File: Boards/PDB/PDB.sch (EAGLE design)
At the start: 47 parts, among them Q1 NMOS, Q2 IRFML8244, Q3 PMOS, Q4 PMOS, Q5 PMOS

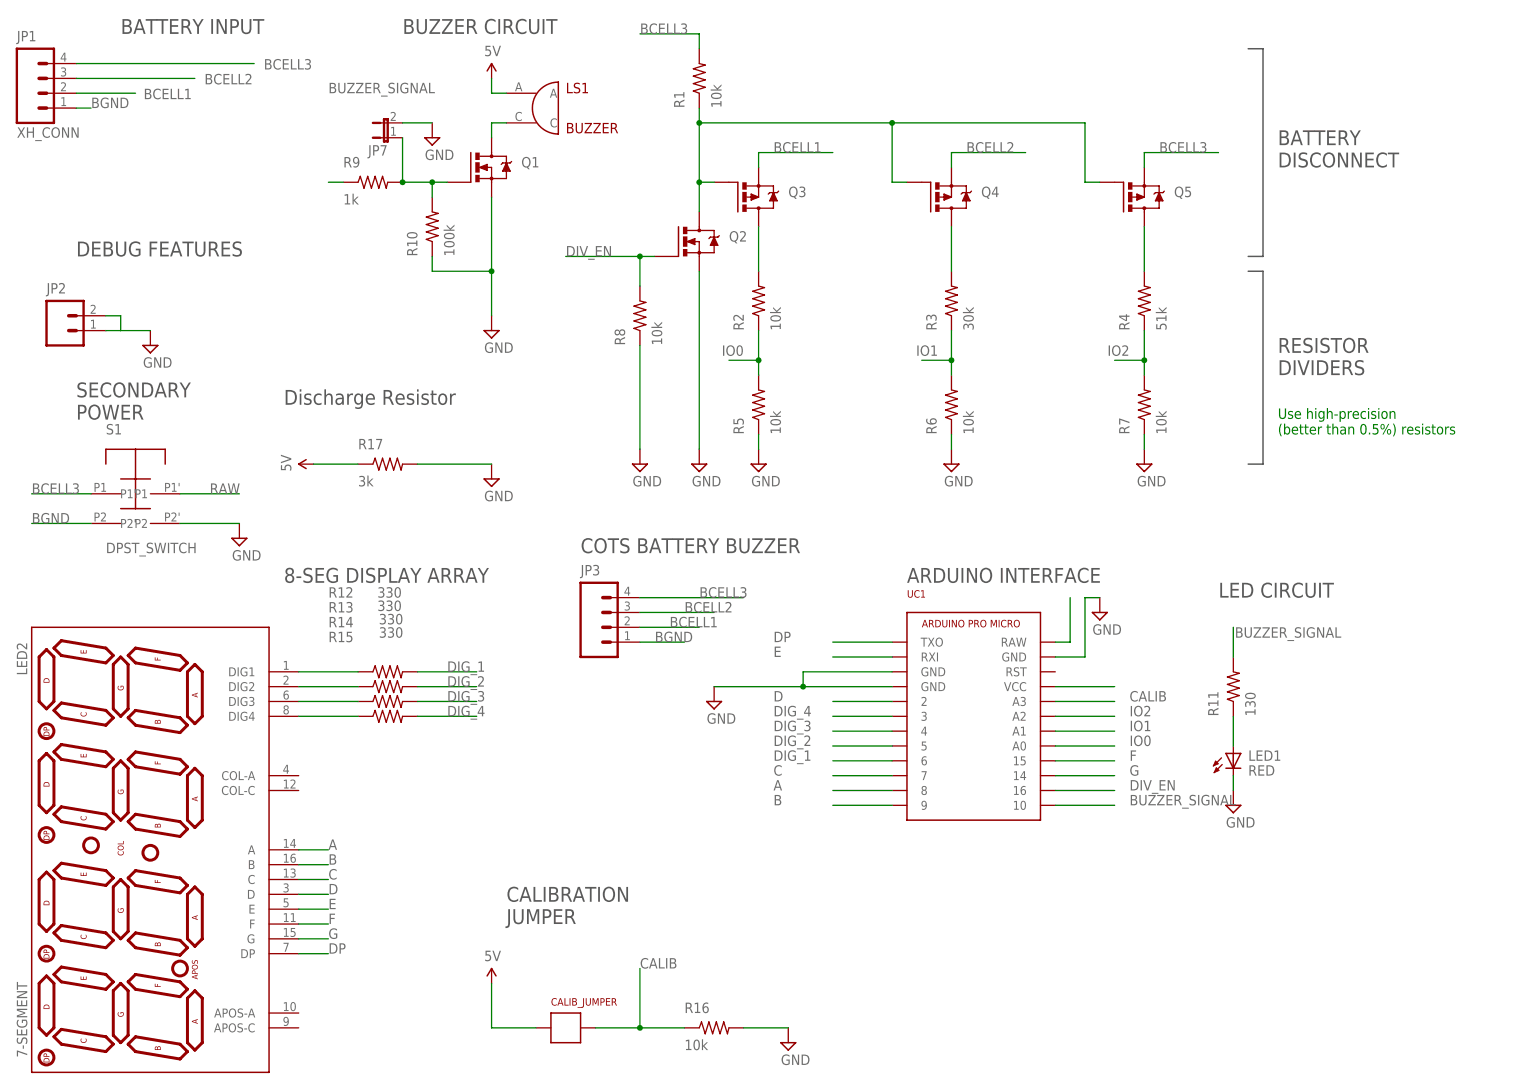
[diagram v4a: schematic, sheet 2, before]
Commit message: Please, PDB, please work. Also I updated ATX connector.
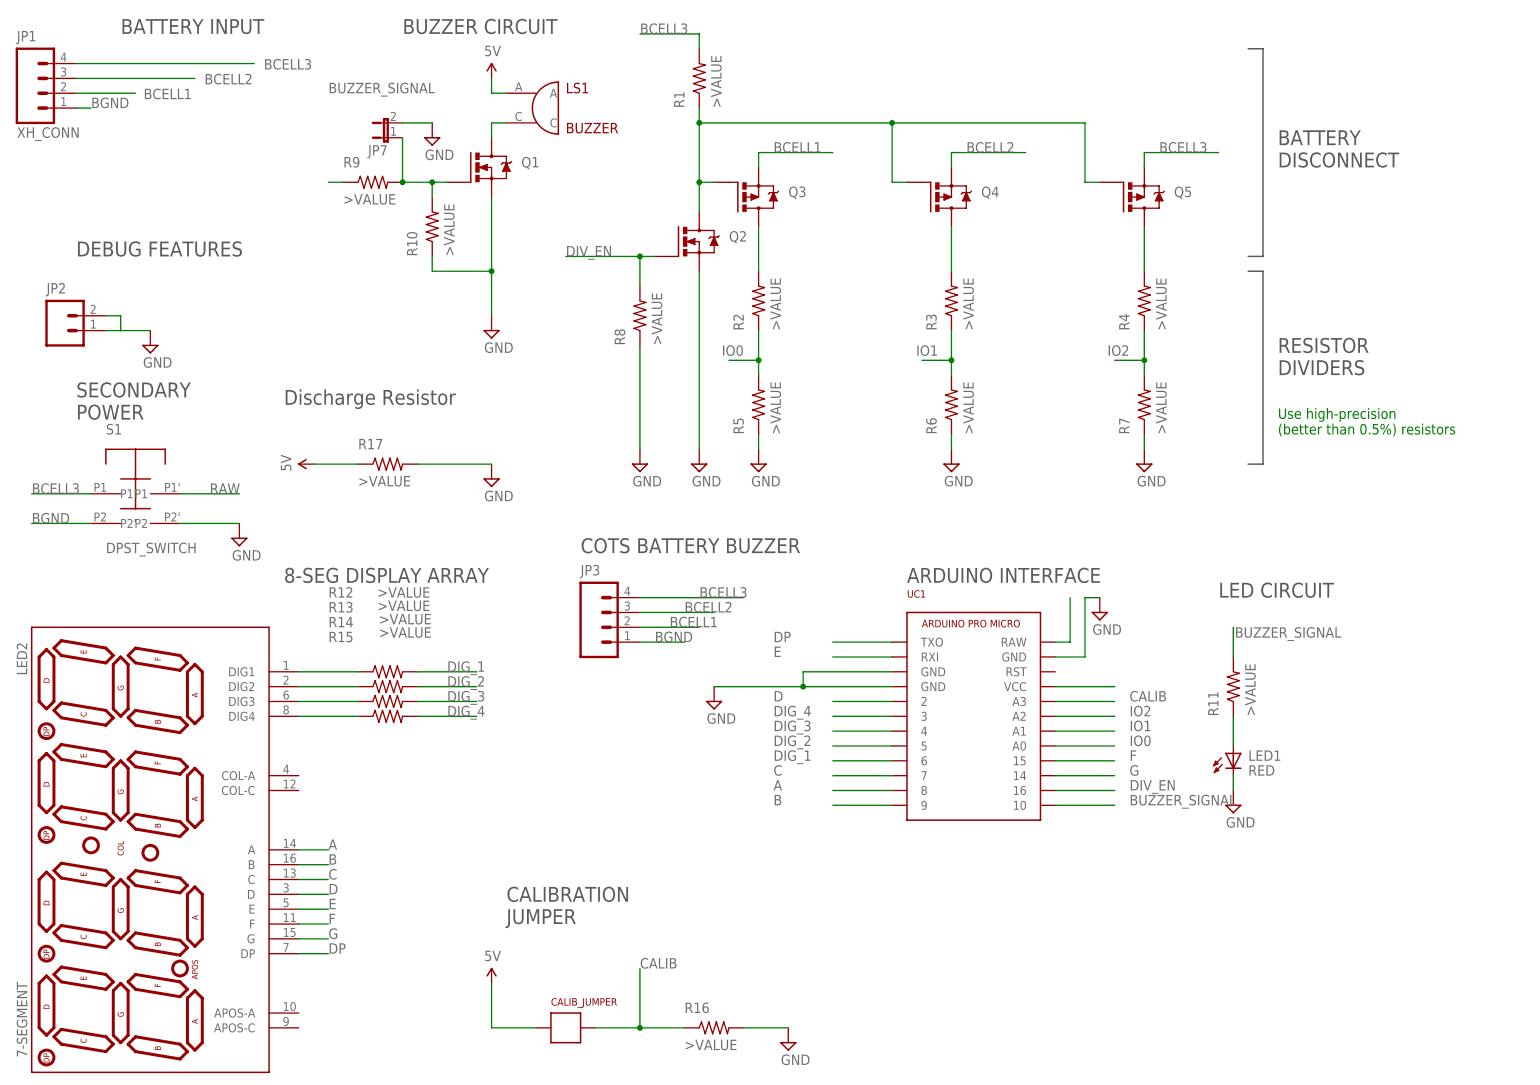
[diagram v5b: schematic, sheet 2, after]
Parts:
- R1, R16, R2, R5, R6, R7, R8: value 10k -> >VALUE
- R10: value 100k -> >VALUE
- R11: value 130 -> >VALUE
- R12, R13, R14, R15: value 330 -> >VALUE
- R17: value 3k -> >VALUE
- R3: value 30k -> >VALUE
- R4: value 51k -> >VALUE
- R9: value 1k -> >VALUE
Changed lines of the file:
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@@
 </part>
 <part name="JP1" library="pie" deviceset="XH_CONNECTOR_4POS" device="" value="XH_CONN"/>
-<part name="R2" library="pie" deviceset="R-US_" device="R0603" value="10k"/>
-<part name="R3" library="pie" deviceset="R-US_" device="R0603" value="30k"/>
-<part name="R4" library="pie" deviceset="R-US_" device="R0603" value="51k"/>
-<part name="R5" library="pie" deviceset="R-US_" device="R0603" value="10k"/>
-<part name="R6" library="pie" deviceset="R-US_" device="R0603" value="10k"/>
-<part name="R7" library="pie" deviceset="R-US_" device="R0603" value="10k"/>
+<part name="R2" library="pie" deviceset="R-US_" device="R0603" value="&gt;VALUE"/>
+<part name="R3" library="pie" deviceset="R-US_" device="R0603" value="&gt;VALUE"/>
+<part name="R4" library="pie" deviceset="R-US_" device="R0603" value="&gt;VALUE"/>
+<part name="R5" library="pie" deviceset="R-US_" device="R0603" value="&gt;VALUE"/>
+<part name="R6" library="pie" deviceset="R-US_" device="R0603" value="&gt;VALUE"/>
+<part name="R7" library="pie" deviceset="R-US_" device="R0603" value="&gt;VALUE"/>
 <part name="SUPPLY14" library="pie" deviceset="GND" device=""/>
 <part name="SUPPLY15" library="pie" deviceset="GND" device=""/>
 <part name="SUPPLY16" library="pie" deviceset="GND" device=""/>
 <part name="LS1" library="pie" deviceset="BUZZER" device="" value="BUZZER"/>
-<part name="R9" library="pie" deviceset="R-US_" device="R0603" value="1k"/>
-<part name="R10" library="pie" deviceset="R-US_" device="R0603" value="100k"/>
+<part name="R9" library="pie" deviceset="R-US_" device="R0603" value="&gt;VALUE"/>
+<part name="R10" library="pie" deviceset="R-US_" device="R0603" value="&gt;VALUE"/>
 <part name="U$12" library="pie" deviceset="5V" device=""/>
 <part name="SUPPLY17" library="pie" deviceset="GND" device=""/>
-<part name="R11" library="pie" deviceset="R-US_" device="R0603" value="130"/>
+<part name="R11" library="pie" deviceset="R-US_" device="R0603" value="&gt;VALUE"/>
 <part name="LED1" library="pie" deviceset="LED" device="0805" value="RED"/>
 <part name="SUPPLY18" library="pie" deviceset="GND" device=""/>
@@
 <part name="Q3" library="pie" deviceset="P-CHANNEL-MOSFET" device="SOT23-3" value="PMOS"/>
 <part name="Q2" library="pie" deviceset="N-CHANNEL-MOSFET" device="SOT23-3" value="IRFML8244"/>
-<part name="R1" library="pie" deviceset="R-US_" device="R0603" value="10k"/>
+<part name="R1" library="pie" deviceset="R-US_" device="R0603" value="&gt;VALUE"/>
 <part name="SUPPLY19" library="pie" deviceset="GND" device=""/>
-<part name="R8" library="pie" deviceset="R-US_" device="R0603" value="10k"/>
+<part name="R8" library="pie" deviceset="R-US_" device="R0603" value="&gt;VALUE"/>
 <part name="SUPPLY20" library="pie" deviceset="GND" device=""/>
 <part name="Q1" library="pie" deviceset="N-CHANNEL-MOSFET" device="SOT23-3" value="NMOS"/>
@@
 <part name="SUPPLY21" library="pie" deviceset="GND" device=""/>
 <part name="SUPPLY22" library="pie" deviceset="GND" device=""/>
-<part name="R13" library="pie" deviceset="R-US_" device="R0603" value="330"/>
-<part name="R14" library="pie" deviceset="R-US_" device="R0603" value="330"/>
-<part name="R12" library="pie" deviceset="R-US_" device="R0603" value="330"/>
-<part name="R15" library="pie" deviceset="R-US_" device="R0603" value="330"/>
+<part name="R13" library="pie" deviceset="R-US_" device="R0603" value="&gt;VALUE"/>
+<part name="R14" library="pie" deviceset="R-US_" device="R0603" value="&gt;VALUE"/>
+<part name="R12" library="pie" deviceset="R-US_" device="R0603" value="&gt;VALUE"/>
+<part name="R15" library="pie" deviceset="R-US_" device="R0603" value="&gt;VALUE"/>
 <part name="U$9" library="pie" deviceset="5V" device=""/>
-<part name="R16" library="pie" deviceset="R-US_" device="R0603" value="10k"/>
+<part name="R16" library="pie" deviceset="R-US_" device="R0603" value="&gt;VALUE"/>
 <part name="SUPPLY23" library="pie" deviceset="GND" device=""/>
 <part name="SUPPLY24" library="pie" deviceset="GND" device=""/>
@@
 <part name="SUPPLY26" library="pie" deviceset="GND" device=""/>
 <part name="APM_5V1" library="pie" deviceset="5V" device=""/>
-<part name="R17" library="pie" deviceset="R-US_" device="R0603" value="3k"/>
-<part name="JP7" library="jumper" deviceset="JP1E" device=""/>
+<part name="R17" library="pie" deviceset="R-US_" device="R0603" value="&gt;VALUE"/>
+<part name="JP7" library="jumper" library_urn="urn:adsk.eagle:library:252" deviceset="JP1E" device="" package3d_urn="urn:adsk.eagle:package:15455/1"/>
 <part name="SUPPLY27" library="pie" deviceset="GND" device=""/>
 <part name="JP3" library="pie" deviceset="M04" device="PTH"/>
@@
 <instance part="SUPPLY12" gate="GND" x="139.7" y="139.7"/>
 <instance part="SUPPLY13" gate="GND" x="177.8" y="139.7"/>
-<instance part="CONN7" gate="CONN$1" x="149.86" y="127" rot="R180"/>
-<instance part="CONN8" gate="CONN$1" x="152.4" y="106.68" rot="R180"/>
-<instance part="CONN9" gate="CONN$1" x="208.28" y="114.3"/>
-<instance part="CONN10" gate="CONN$1" x="208.28" y="91.44"/>
+<instance part="CONN7" gate="G$1" x="149.86" y="127" rot="R180"/>
+<instance part="CONN8" gate="G$1" x="152.4" y="106.68" rot="R180"/>
+<instance part="CONN9" gate="G$1" x="208.28" y="114.3"/>
+<instance part="CONN10" gate="G$1" x="208.28" y="91.44"/>
 <instance part="C1" gate="G$1" x="22.86" y="71.12"/>
 <instance part="C2" gate="G$1" x="38.1" y="71.12"/>
@@
 <pinref part="SUPPLY9" gate="GND" pin="GND"/>
 <wire x1="198.12" y1="109.22" x2="193.04" y2="109.22" width="0.1524" layer="91"/>
-<pinref part="CONN9" gate="CONN$1" pin="P$2"/>
+<pinref part="CONN9" gate="G$1" pin="P$2"/>
 </segment>
 <segment>
@@
 <pinref part="SUPPLY10" gate="GND" pin="GND"/>
 <wire x1="160.02" y1="132.08" x2="170.18" y2="132.08" width="0.1524" layer="91"/>
-<pinref part="CONN7" gate="CONN$1" pin="P$2"/>
+<pinref part="CONN7" gate="G$1" pin="P$2"/>
 </segment>
 <segment>
 <pinref part="SUPPLY11" gate="GND" pin="GND"/>
 <wire x1="162.56" y1="111.76" x2="170.18" y2="111.76" width="0.1524" layer="91"/>
-<pinref part="CONN8" gate="CONN$1" pin="P$2"/>
+<pinref part="CONN8" gate="G$1" pin="P$2"/>
 </segment>
 <segment>
 <pinref part="SUPPLY8" gate="GND" pin="GND"/>
 <wire x1="198.12" y1="86.36" x2="193.04" y2="86.36" width="0.1524" layer="91"/>
-<pinref part="CONN10" gate="CONN$1" pin="P$2"/>
+<pinref part="CONN10" gate="G$1" pin="P$2"/>
 </segment>
 <segment>
@@
 <net name="5V" class="0">
 <segment>
-<pinref part="CONN10" gate="CONN$1" pin="P$1"/>
-<pinref part="CONN8" gate="CONN$1" pin="P$1"/>
-<pinref part="CONN9" gate="CONN$1" pin="P$1"/>
-<pinref part="CONN7" gate="CONN$1" pin="P$1"/>
+<pinref part="CONN10" gate="G$1" pin="P$1"/>
+<pinref part="CONN8" gate="G$1" pin="P$1"/>
+<pinref part="CONN9" gate="G$1" pin="P$1"/>
+<pinref part="CONN7" gate="G$1" pin="P$1"/>
 <wire x1="182.88" y1="124.46" x2="160.02" y2="124.46" width="0.1524" layer="91"/>
 <wire x1="175.26" y1="147.32" x2="182.88" y2="147.32" width="0.1524" layer="91"/>

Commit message: I hate my life
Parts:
- R1, R16, R2, R5, R6, R7, R8: value >VALUE -> 10k
- R10: value >VALUE -> 100k
- R11: value >VALUE -> 130
- R12, R13, R14, R15: value >VALUE -> 330
- R17: value >VALUE -> 3k
- R3: value >VALUE -> 30k
- R4: value >VALUE -> 51k
- R9: value >VALUE -> 1k
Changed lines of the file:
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@@
 <parts>
 <part name="FRAME1" library="pie" deviceset="FRAME_SCHEMATIC" device="">
-<attribute name="AUTHOR" value="Mohammed H., Sharabesh R., Tobin H."/>
-<attribute name="REVISION" value="10C"/>
+<attribute name="AUTHOR" value="Tobin H, Nick W, Adilet P"/>
+<attribute name="REVISION" value="PROD"/>
 </part>
 <part name="XT60" library="pie" deviceset="XT60CONNECTOR" device=""/>
@@
 <part name="SUPPLY13" library="pie" deviceset="GND" device=""/>
 <part name="FRAME2" library="pie" deviceset="FRAME_SCHEMATIC" device="">
-<attribute name="AUTHOR" value="Casey D, Douglas H, Mohammed H, Tobin H"/>
-<attribute name="REVISION" value="10C"/>
+<attribute name="AUTHOR" value="Casey D, Douglas H, Nick W, Tobin H"/>
+<attribute name="REVISION" value="PROD"/>
 </part>
 <part name="JP1" library="pie" deviceset="XH_CONNECTOR_4POS" device="" value="XH_CONN"/>
-<part name="R2" library="pie" deviceset="R-US_" device="R0603" value="&gt;VALUE"/>
-<part name="R3" library="pie" deviceset="R-US_" device="R0603" value="&gt;VALUE"/>
-<part name="R4" library="pie" deviceset="R-US_" device="R0603" value="&gt;VALUE"/>
-<part name="R5" library="pie" deviceset="R-US_" device="R0603" value="&gt;VALUE"/>
-<part name="R6" library="pie" deviceset="R-US_" device="R0603" value="&gt;VALUE"/>
-<part name="R7" library="pie" deviceset="R-US_" device="R0603" value="&gt;VALUE"/>
+<part name="R2" library="pie" deviceset="R-US_" device="R0603" value="10k"/>
+<part name="R3" library="pie" deviceset="R-US_" device="R0603" value="30k"/>
+<part name="R4" library="pie" deviceset="R-US_" device="R0603" value="51k"/>
+<part name="R5" library="pie" deviceset="R-US_" device="R0603" value="10k"/>
+<part name="R6" library="pie" deviceset="R-US_" device="R0603" value="10k"/>
+<part name="R7" library="pie" deviceset="R-US_" device="R0603" value="10k"/>
 <part name="SUPPLY14" library="pie" deviceset="GND" device=""/>
 <part name="SUPPLY15" library="pie" deviceset="GND" device=""/>
 <part name="SUPPLY16" library="pie" deviceset="GND" device=""/>
 <part name="LS1" library="pie" deviceset="BUZZER" device="" value="BUZZER"/>
-<part name="R9" library="pie" deviceset="R-US_" device="R0603" value="&gt;VALUE"/>
-<part name="R10" library="pie" deviceset="R-US_" device="R0603" value="&gt;VALUE"/>
+<part name="R9" library="pie" deviceset="R-US_" device="R0603" value="1k"/>
+<part name="R10" library="pie" deviceset="R-US_" device="R0603" value="100k"/>
 <part name="U$12" library="pie" deviceset="5V" device=""/>
 <part name="SUPPLY17" library="pie" deviceset="GND" device=""/>
-<part name="R11" library="pie" deviceset="R-US_" device="R0603" value="&gt;VALUE"/>
+<part name="R11" library="pie" deviceset="R-US_" device="R0603" value="130"/>
 <part name="LED1" library="pie" deviceset="LED" device="0805" value="RED"/>
 <part name="SUPPLY18" library="pie" deviceset="GND" device=""/>
@@
 <part name="Q3" library="pie" deviceset="P-CHANNEL-MOSFET" device="SOT23-3" value="PMOS"/>
 <part name="Q2" library="pie" deviceset="N-CHANNEL-MOSFET" device="SOT23-3" value="IRFML8244"/>
-<part name="R1" library="pie" deviceset="R-US_" device="R0603" value="&gt;VALUE"/>
+<part name="R1" library="pie" deviceset="R-US_" device="R0603" value="10k"/>
 <part name="SUPPLY19" library="pie" deviceset="GND" device=""/>
-<part name="R8" library="pie" deviceset="R-US_" device="R0603" value="&gt;VALUE"/>
+<part name="R8" library="pie" deviceset="R-US_" device="R0603" value="10k"/>
 <part name="SUPPLY20" library="pie" deviceset="GND" device=""/>
 <part name="Q1" library="pie" deviceset="N-CHANNEL-MOSFET" device="SOT23-3" value="NMOS"/>
@@
 <part name="SUPPLY21" library="pie" deviceset="GND" device=""/>
 <part name="SUPPLY22" library="pie" deviceset="GND" device=""/>
-<part name="R13" library="pie" deviceset="R-US_" device="R0603" value="&gt;VALUE"/>
-<part name="R14" library="pie" deviceset="R-US_" device="R0603" value="&gt;VALUE"/>
-<part name="R12" library="pie" deviceset="R-US_" device="R0603" value="&gt;VALUE"/>
-<part name="R15" library="pie" deviceset="R-US_" device="R0603" value="&gt;VALUE"/>
+<part name="R13" library="pie" deviceset="R-US_" device="R0603" value="330"/>
+<part name="R14" library="pie" deviceset="R-US_" device="R0603" value="330"/>
+<part name="R12" library="pie" deviceset="R-US_" device="R0603" value="330"/>
+<part name="R15" library="pie" deviceset="R-US_" device="R0603" value="330"/>
 <part name="U$9" library="pie" deviceset="5V" device=""/>
-<part name="R16" library="pie" deviceset="R-US_" device="R0603" value="&gt;VALUE"/>
+<part name="R16" library="pie" deviceset="R-US_" device="R0603" value="10k"/>
 <part name="SUPPLY23" library="pie" deviceset="GND" device=""/>
 <part name="SUPPLY24" library="pie" deviceset="GND" device=""/>
@@
 <part name="SUPPLY26" library="pie" deviceset="GND" device=""/>
 <part name="APM_5V1" library="pie" deviceset="5V" device=""/>
-<part name="R17" library="pie" deviceset="R-US_" device="R0603" value="&gt;VALUE"/>
+<part name="R17" library="pie" deviceset="R-US_" device="R0603" value="3k"/>
 <part name="JP7" library="jumper" library_urn="urn:adsk.eagle:library:252" deviceset="JP1E" device="" package3d_urn="urn:adsk.eagle:package:15455/1"/>
 <part name="SUPPLY27" library="pie" deviceset="GND" device=""/>
